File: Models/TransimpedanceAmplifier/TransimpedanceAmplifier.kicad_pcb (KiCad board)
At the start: 2 copper layers, 107 parts, among them J1 Conn_01x02_Socket, J10 Conn_01x02_Pin, J11 Conn_01x24_Socket, J14 Conn_01x24_Socket, J2 Conn_01x02_Socket, J3 Conn_01x03_Pin, J4 Conn_01x02_Pin, J5 Conn_01x02_Pin, J6 Conn_01x02_Pin, J7 Conn_01x02_Pin, J8 Conn_01x02_Pin, J9 Conn_01x02_Pin, Q1 Q_PNP, Q2 Q_NPN, U1 LM7905, -5V, 5%, U10 DAC81401, U11 ISO7641FM, U12 ISO7641FM, U13 ADS8699, U2 LM7805, 5V, 5%, U3 OPA828, U4 AD8615, U5 OP37GPZ, U6 LM7915, -15V, 5%, U7 LM7815, 15V, 5%, U8 LM7805, 5V, 5%, U9 TLV76133, 3.3V, 1%

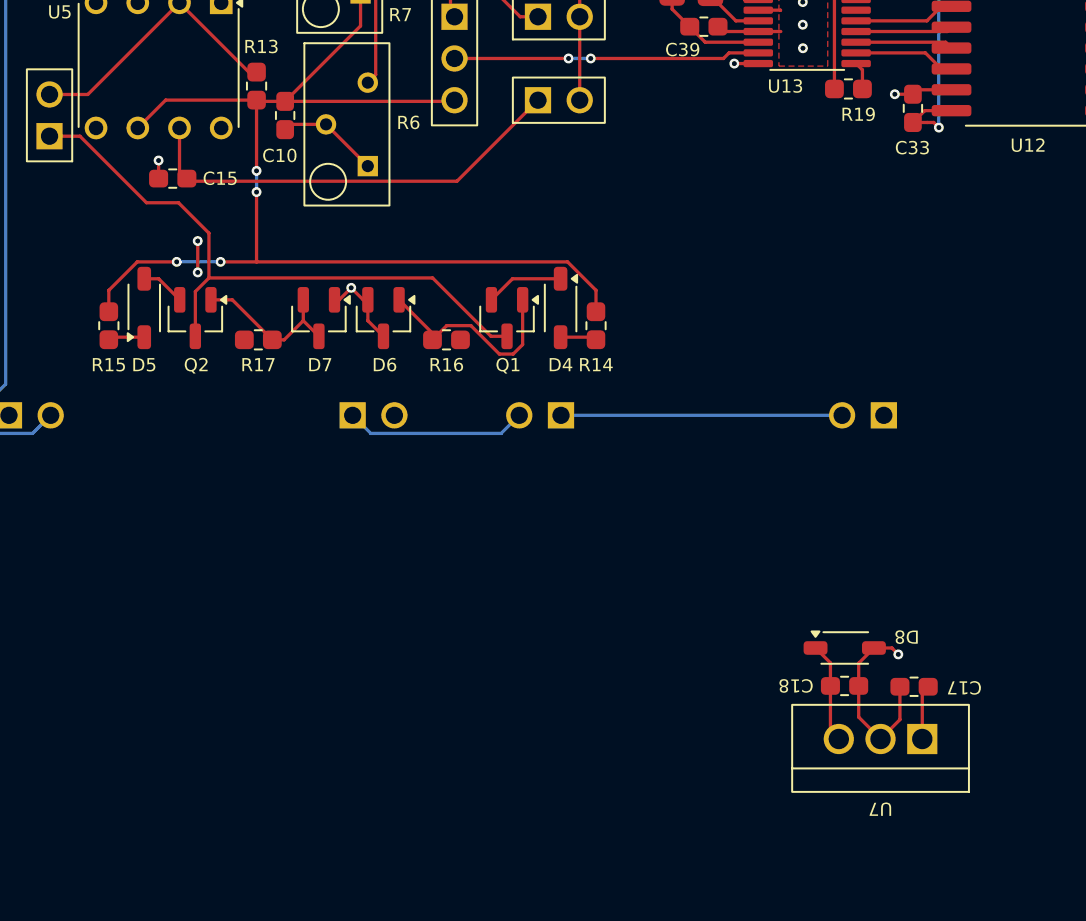
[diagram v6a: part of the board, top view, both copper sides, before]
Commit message: Started routing a few of the 15 V power traces
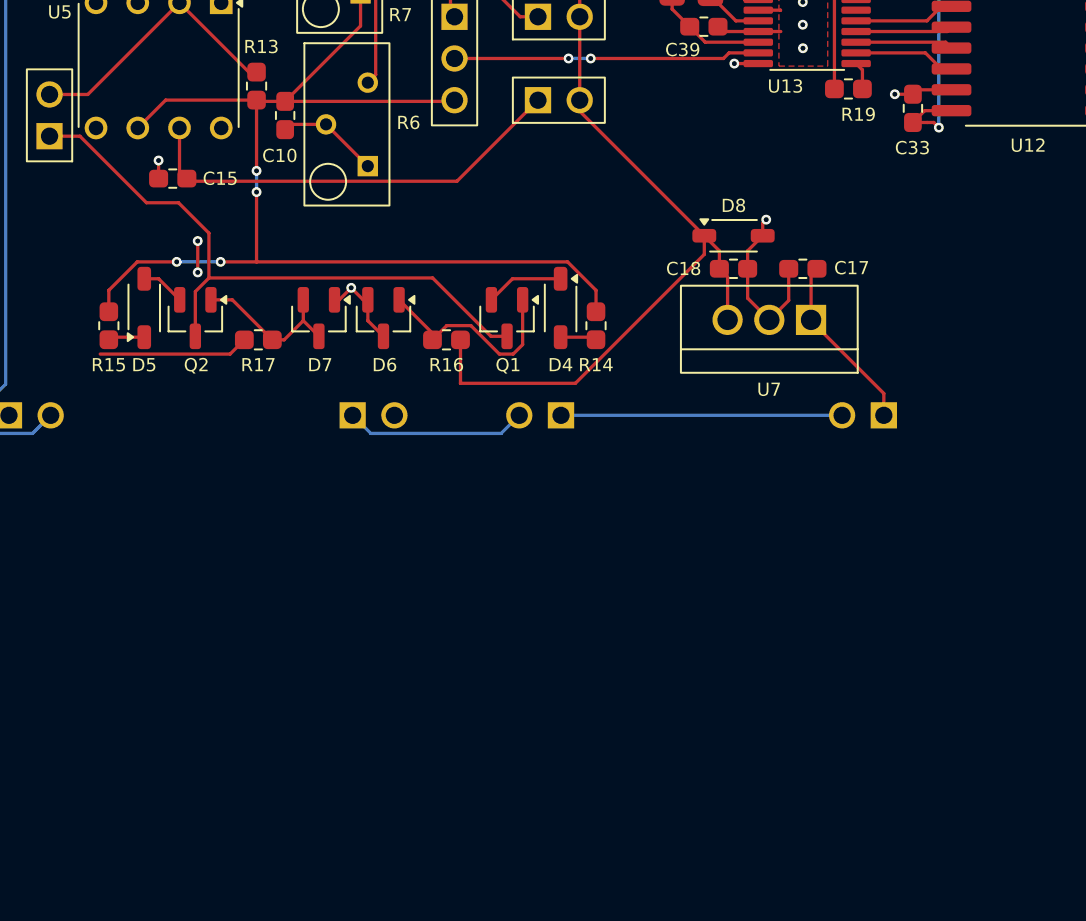
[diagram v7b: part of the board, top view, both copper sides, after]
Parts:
- moved U7 26.4 mm to (122.4, 127.0)
- moved C17 26.3 mm to (124.5, 123.9)
- moved C18 26.3 mm to (120.2, 123.9)
- moved D8 26.0 mm to (120.2, 121.8)
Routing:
- net /15V: track 32.1 -> 65.0 mm
- net /-15V: track 11.2 -> 20.3 mm
- net /Power/Batteries/27V: track 3.32 -> 10.9 mm
- net GND: track 134.8 -> 133.7 mm
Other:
- board text removed: "15 V"
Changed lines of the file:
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@@
 	(footprint "ThreeTerminal:TO-220"
 		(layer "F.Cu")
-		(at 129.19 152.48 180)
+		(at 122.42 126.97 180)
 		(property "Reference" "U7"
-			(at 0.01 -4.25 180)
+			(at 0.01 -4.25 0)
 			(unlocked yes)
 			(layer "F.SilkS")
@@
 	(footprint "TwoTerminal:CAPC0603"
 		(layer "F.Cu")
-		(at 131.23 149.3 180)
+		(at 124.46 123.86 180)
 		(property "Reference" "C17"
-			(at -3.05 -0.04 180)
+			(at -2.98 0.04 0)
 			(unlocked yes)
 			(layer "F.SilkS")
@@
 	(footprint "TwoTerminal:CAPC0603"
 		(layer "F.Cu")
-		(at 127 149.25)
+		(at 120.24 123.86)
 		(property "Reference" "C18"
-			(at -2.96 -0.03 180)
+			(at -3.03 0.01 0)
 			(unlocked yes)
 			(layer "F.SilkS")
@@
 	(footprint "TwoTerminal:SOD-123"
 		(layer "F.Cu")
-		(at 127.01 146.94)
+		(at 120.24 121.85)
 		(property "Reference" "D8"
-			(at 3.78 -0.69 180)
+			(at 0.01 -1.82 0)
 			(unlocked yes)
 			(layer "F.SilkS")
@@
 		)
 	)
-	(gr_text "15 V"
-		(at 137.33 152.75 180)
-		(layer "User.2")
-		(effects
-			(font
-				(size 0.8 0.8)
-				(thickness 0.12)
-			)
-			(justify left bottom)
-		)
-	)
 	(gr_text "-1.5 V"
 		(at 29.57 52.39 90)
@@
 	)
 	(segment
-		(start 131.73 149.66)
-		(end 132.09 149.3)
+		(start 124.96 126.97)
+		(end 124.96 124.22)
+		(width 0.2)
+		(layer "F.Cu")
+		(net 4)
+	)
+	(segment
+		(start 129.39 131.45)
+		(end 129.39 132.78)
+		(width 0.2)
+		(layer "F.Cu")
+		(net 4)
+	)
+	(segment
+		(start 124.96 127.02)
+		(end 129.39 131.45)
+		(width 0.2)
+		(layer "F.Cu")
+		(net 4)
+	)
+	(segment
+		(start 124.96 124.22)
+		(end 125.32 123.86)
 		(width 0.2)
 		(layer "F.Cu")
@@
 	)
 	(segment
-		(start 131.73 152.47)
-		(end 131.73 149.66)
+		(start 124.96 126.97)
+		(end 124.96 127.02)
 		(width 0.2)
 		(layer "F.Cu")
@@
 	)
 	(segment
+		(start 121.1 125.65)
+		(end 122.42 126.97)
+		(width 0.2)
+		(layer "F.Cu")
+		(net 5)
+	)
+	(segment
 		(start 127.005 89.50858)
 		(end 127.535 90.03858)
@@
 	)
 	(segment
-		(start 130.37 149.3)
-		(end 130.37 151.3)
-		(width 0.2)
-		(layer "F.Cu")
-		(net 5)
-	)
-	(segment
 		(start 126.7475 105.405)
 		(end 125.3475 106.805)
@@
 	)
 	(segment
-		(start 130.37 151.3)
-		(end 129.19 152.48)
-		(width 0.2)
-		(layer "F.Cu")
-		(net 5)
-	)
-	(segment
 		(start 117.545 89.635)
 		(end 116.395 89.635)
@@
 	)
 	(segment
-		(start 128.7875 146.94)
-		(end 129.88 146.94)
-		(width 0.2)
-		(layer "F.Cu")
-		(net 5)
-	)
-	(segment
 		(start 116.505 105.19179)
 		(end 116.7575 105.19179)
@@
 	)
 	(segment
+		(start 122.0175 121.0825)
+		(end 122.23 120.87)
+		(width 0.2)
+		(layer "F.Cu")
+		(net 5)
+	)
+	(segment
 		(start 144.65 56.38)
 		(end 144.65 57.7625)
@@
 	)
 	(segment
+		(start 122.0175 121.85)
+		(end 122.0175 121.0825)
+		(width 0.2)
+		(layer "F.Cu")
+		(net 5)
+	)
+	(segment
 		(start 120.84179 90.985)
 		(end 121.305 90.52179)
@@
 	)
 	(segment
+		(start 121.1 123.86)
+		(end 121.1 122.7675)
+		(width 0.2)
+		(layer "F.Cu")
+		(net 5)
+	)
+	(segment
 		(start 83.7525 63.98)
 		(end 82.7 63.98)
@@
 	)
 	(segment
+		(start 121.1 122.7675)
+		(end 122.0175 121.85)
+		(width 0.2)
+		(layer "F.Cu")
+		(net 5)
+	)
+	(segment
 		(start 127.535 90.03858)
 		(end 128.55179 90.03858)
@@
 	)
 	(segment
+		(start 121.1 123.86)
+		(end 121.1 125.65)
+		(width 0.2)
+		(layer "F.Cu")
+		(net 5)
+	)
+	(segment
 		(start 160.59 60.1775)
 		(end 162.055 60.1775)
@@
 	)
 	(segment
-		(start 127.86 149.25)
-		(end 127.86 147.8675)
-		(width 0.2)
-		(layer "F.Cu")
-		(net 5)
-	)
-	(segment
 		(start 80.5025 97.5875)
 		(end 80.37 97.72)
@@
 	)
 	(segment
-		(start 127.86 149.25)
-		(end 127.86 151.15)
-		(width 0.2)
-		(layer "F.Cu")
-		(net 5)
-	)
-	(segment
 		(start 143.96 30.08125)
 		(end 143.96 31.84375)
@@
 	)
 	(segment
-		(start 127.86 147.8675)
-		(end 128.7875 146.94)
-		(width 0.2)
-		(layer "F.Cu")
-		(net 5)
-	)
-	(segment
 		(start 131.43 112.965)
 		(end 131.16 113.235)
@@
 	)
 	(segment
-		(start 143.96 31.84375)
-		(end 143.96 33.2975)
+		(start 123.6 123.86)
+		(end 123.6 125.79)
 		(width 0.2)
 		(layer "F.Cu")
@@
 	)
 	(segment
-		(start 119.295 109.12429)
-		(end 119.59 109.41929)
+		(start 143.96 31.84375)
+		(end 143.96 33.2975)
 		(width 0.2)
 		(layer "F.Cu")
@@
 	)
 	(segment
-		(start 127.86 151.15)
-		(end 129.19 152.48)
+		(start 119.295 109.12429)
+		(end 119.59 109.41929)
 		(width 0.2)
 		(layer "F.Cu")
@@
 	)
 	(segment
-		(start 133.51 105.345)
-		(end 131.74 105.345)
+		(start 123.6 125.79)
+		(end 122.42 126.97)
 		(width 0.2)
 		(layer "F.Cu")
@@
 	)
 	(segment
-		(start 129.88 146.94)
-		(end 130.27 147.33)
+		(start 133.51 105.345)
+		(end 131.74 105.345)
 		(width 0.2)
 		(layer "F.Cu")
@@
 	)
 	(via
+		(at 122.23 120.87)
+		(size 0.6)
+		(drill 0.3)
+		(layers "F.Cu" "B.Cu")
+		(net 5)
+	)
+	(via
 		(at 87.63 122.17)
 		(size 0.6)
@@
 	)
 	(via
-		(at 130.27 147.33)
-		(size 0.6)
-		(drill 0.3)
-		(layers "F.Cu" "B.Cu")
-		(net 5)
-	)
-	(via
 		(at 82.28 63.56)
 		(size 0.6)
@@
 	)
 	(segment
-		(start 126.14 147.8475)
-		(end 125.2325 146.94)
-		(width 0.2)
-		(layer "F.Cu")
-		(net 10)
-	)
-	(segment
-		(start 126.14 149.25)
-		(end 126.14 147.8475)
+		(start 118.4625 121.85)
+		(end 118.4625 122.984027)
 		(width 0.2)
 		(layer "F.Cu")
@@
 	)
 	(segment
-		(start 126.14 149.25)
-		(end 126.14 151.96)
+		(start 103.62 130.83)
+		(end 103.622833 130.827167)
 		(width 0.2)
 		(layer "F.Cu")
@@
 	)
 	(segment
-		(start 126.14 151.97)
-		(end 126.65 152.48)
+		(start 110.616527 130.83)
+		(end 103.62 130.83)
 		(width 0.2)
 		(layer "F.Cu")
@@
 	)
 	(segment
+		(start 119.38 123.86)
+		(end 119.38 122.7675)
+		(width 0.2)
+		(layer "F.Cu")
+		(net 10)
+	)
+	(segment
 		(start 114.429 97.451)
 		(end 114.429 94.721)
@@
 	)
 	(segment
+		(start 119.38 122.7675)
+		(end 118.4625 121.85)
+		(width 0.2)
+		(layer "F.Cu")
+		(net 10)
+	)
+	(segment
 		(start 80.9 61.23)
 		(end 80.34 61.79)
@@
 	)
 	(segment
+		(start 118.4625 122.984027)
+		(end 110.616527 130.83)
+		(width 0.2)
+		(layer "F.Cu")
+		(net 10)
+	)
+	(segment
+		(start 119.88 126.97)
+		(end 119.88 124.36)
+		(width 0.2)
+		(layer "F.Cu")
+		(net 10)
+	)
+	(segment
 		(start 80.9 58.64)
 		(end 80.9 61.23)
@@
 	)
 	(segment
+		(start 119.88 124.36)
+		(end 119.38 123.86)
+		(width 0.2)
+		(layer "F.Cu")
+		(net 10)
+	)
+	(segment
 		(start 110.88 108.52)
 		(end 110.88 101)
@@
 	)
 	(segment
+		(start 118.4625 121.85)
+		(end 110.88 114.2675)
+		(width 0.2)
+		(layer "F.Cu")
+		(net 10)
+	)
+	(segment
+		(start 110.88 114.2675)
+		(end 110.88 113.6)
+		(width 0.2)
+		(layer "F.Cu")
+		(net 10)
+	)
+	(segment
+		(start 103.622833 130.827167)
+		(end 103.622833 128.185)
+		(width 0.2)
+		(layer "F.Cu")
+		(net 10)
+	)
+	(segment
 		(start 86.4 59.06)
 		(end 85.98 58.64)
@@
 		(width 0.2)
 		(layer "F.Cu")
+		(net 13)
+	)
+	(segment
+		(start 89.600833 129.051)
+		(end 81.694139 129.051)
+		(width 0.2)
+		(layer "F.Cu")
+		(net 13)
+	)
+	(segment
+		(start 90.466833 128.185)
+		(end 89.600833 129.051)
+		(width 0.2)
+		(layer "F.Cu")

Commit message: Resolved another round of unknowns
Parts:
- moved J10 88.5 mm to (78.1, 106.4)
- moved J9 0.69 mm to (78.1, 114.0)
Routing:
- net /-15V: track 20.3 -> 46.3 mm
- net /TIA_TwoStage/PostAmplifier/V-: track 3.20 -> 6.26 mm
- net /TIA_TwoStage/PostAmplifier/Clamped_Output: track 38.4 -> 39.1 mm
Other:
- board text removed: "Bring -15 V all the way around from top of board with long trace on left edge. Topology-wise, from left to right: Conductor connecting two battery terminals -15 V trace (transporting power to bottom) 15 V trace (transporting power to top) Either ordering of -15 V vs. 15 V has an unsavory crossover. Choose the best one after more relevant information is known."
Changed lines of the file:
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@@
 	)
 	(footprint "ThreeTerminal:TO-220"
+		(locked yes)
 		(layer "F.Cu")
 		(at 122.42 126.97 180)
@@
 		(at 85.25 111.48 -90)
 		(property "Reference" "U5"
-			(at -3.23 6.01 0)
+			(at -3.74 -6.1 0)
 			(unlocked yes)
 			(layer "F.SilkS")
@@
 	)
 	(footprint "TwoTerminal:CAPC0603"
+		(locked yes)
 		(layer "F.Cu")
 		(at 124.46 123.86 180)
@@
 		(locked yes)
 		(layer "F.Cu")
-		(at 78.61 114.52 180)
+		(at 78.14 114.02 180)
 		(property "Reference" "J9"
 			(at 0.73 3.63 0)
@@
 	)
 	(footprint "TwoTerminal:CAPC0603"
+		(locked yes)
 		(layer "F.Cu")
 		(at 120.24 123.86)
@@
 	)
 	(footprint "TwoTerminal:SOD-123"
+		(locked yes)
 		(layer "F.Cu")
 		(at 120.24 121.85)
@@
 	)
 	(footprint "Connector_Custom:PinHeader_1x2"
+		(locked yes)
 		(layer "F.Cu")
-		(at 23.39 175.99)
+		(at 78.14 106.4)
 		(property "Reference" "J10"
 			(at 0.0025 -3.5625 0)
@@
 	)
 	(footprint "TwoTerminal:CAPC0603"
-		(locked yes)
 		(layer "F.Cu")
 		(at 81.8575 104.65)
 		(property "Reference" "C16"
-			(at -3.1775 0.04 0)
+			(at -0.6175 -1.51 0)
 			(unlocked yes)
 			(layer "F.SilkS")
@@
 		)
 	)
-	(gr_text "Bring -15 V all the way around from top\nof board with long trace on left edge.\n\nTopology-wise, from left to right:\nConductor connecting two battery terminals\n-15 V trace (transporting power to bottom)\n15 V trace (transporting power to top)\n\nEither ordering of -15 V vs. 15 V has an\nunsavory crossover. Choose the best one\nafter more relevant information is known."
-		(at 43.77 120.98 0)
-		(layer "User.2")
-		(effects
-			(font
-				(size 0.8 0.8)
-				(thickness 0.12)
-			)
-			(justify left top)
-		)
-	)
 	(gr_text "-27 V"
 		(at 96.87 53.73 0)
@@
 	)
 	(segment
+		(start 81.694139 129.051)
+		(end 75.94 123.296861)
+		(width 0.2)
+		(layer "F.Cu")
+		(net 13)
+	)
+	(segment
 		(start 145.965 31.84375)
 		(end 145.965 33.2775)
@@
 	)
 	(segment
+		(start 75.94 107.67)
+		(end 78.14 107.67)
+		(width 0.2)
+		(layer "F.Cu")
+		(net 13)
+	)
+	(segment
 		(start 145.965 30.02125)
 		(end 145.965 31.84375)
@@
 	)
 	(segment
+		(start 75.94 123.296861)
+		(end 75.94 107.67)
+		(width 0.2)
+		(layer "F.Cu")
+		(net 13)
+	)
+	(segment
 		(start 104.5025 105.765)
 		(end 104.505 105.765)
@@
 	)
 	(segment
+		(start 78.14 105.13)
+		(end 80.5175 105.13)
+		(width 0.2)
+		(layer "F.Cu")
+		(net 23)
+	)
+	(segment
+		(start 80.5175 105.13)
+		(end 80.9975 104.65)
+		(width 0.2)
+		(layer "F.Cu")
+		(net 23)
+	)
+	(segment
 		(start 81.44 105.0925)
 		(end 80.9975 104.65)
@@
 	)
 	(segment
-		(start 80.46 115.79)
-		(end 84.51 119.84)
-		(width 0.2)
-		(layer "F.Cu")
-		(net 54)
-	)
-	(segment
 		(start 84.51 119.84)
 		(end 86.46 119.84)
@@
 	)
 	(segment
-		(start 78.61 115.79)
-		(end 80.46 115.79)
+		(start 78.14 115.29)
+		(end 79.96 115.29)
 		(width 0.2)
 		(layer "F.Cu")
@@
 	)
 	(segment
+		(start 79.96 115.29)
+		(end 84.51 119.84)
+		(width 0.2)
+		(layer "F.Cu")
+		(net 54)
+	)
+	(segment
 		(start 106.455666 127.97)
 		(end 105.4771 127.97)
@@
 	)
 	(segment
-		(start 86.52 107.67)
-		(end 90.7375 111.8875)
+		(start 81.44 112.75)
+		(end 86.52 107.67)
 		(width 0.2)
 		(layer "F.Cu")
@@
 	)
 	(segment
-		(start 80.94 113.25)
-		(end 78.61 113.25)
+		(start 86.52 107.67)
+		(end 90.7375 111.8875)
 		(width 0.2)
 		(layer "F.Cu")
@@
 	)
 	(segment
-		(start 86.52 107.67)
-		(end 80.94 113.25)
+		(start 78.14 112.75)
+		(end 81.44 112.75)
 		(width 0.2)
 		(layer "F.Cu")
